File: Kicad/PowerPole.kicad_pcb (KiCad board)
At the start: 2 copper layers, 198.1 x 116.8 mm, 41 parts, among them J1 Anderson powerpole, J2 Anderson powerpole, J3 Anderson powerpole, J4 Anderson powerpole, J5 Anderson powerpole, K1 896HP-1AH-C-12VDC, SW1 SW_Push

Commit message: PCB update
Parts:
- added J6: Meter +ve, Connector_Wire:SolderWire-0.5sqmm_1x01_D0.9mm_OD2.1mm, F.Cu at (124.5, 45.7)
- added J7: Meter GND, Connector_Wire:SolderWire-2.5sqmm_1x01_D2.4mm_OD4.4mm, F.Cu at (98.4, 57.8)
- added J8: Meter LOAD, Connector_Wire:SolderWire-2.5sqmm_1x01_D2.4mm_OD4.4mm, F.Cu at (108.0, 57.8)
- moved D3 86.0 mm to (187.3, 77.5), turned to 90 degrees
- moved R2 79.9 mm to (187.3, 66.7), turned to 90 degrees
- moved D2 74.3 mm to (183.5, 38.1), turned to 0 degrees
- moved R1 73.3 mm to (193.7, 67.3)
- moved C2 67.9 mm to (194.3, 38.1)
- moved C1 60.3 mm to (193.0, 57.1)
- moved C4 51.7 mm to (184.8, 52.1), turned to 90 degrees
- moved D7 51.6 mm to (168.9, 85.1)
- moved D9 51.6 mm to (127.0, 85.1)
- moved F4 51.6 mm to (139.7, 85.1)
- moved F5 51.6 mm to (158.8, 85.1)
- moved D10 51.6 mm to (108.0, 85.1)
- moved F2 51.6 mm to (97.8, 85.1)
- moved D8 51.6 mm to (149.9, 85.1)
- moved F3 51.6 mm to (116.8, 85.1)
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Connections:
- net Net-(D1-Pad2) renamed /Vout
- C1 pad 2: Net-(C1-Pad2) -> /GND
- C2 pad 2: Net-(C1-Pad2) -> /GND
- C3 pad 2: Net-(C1-Pad2) -> /GND
- C4 pad 2: Net-(C1-Pad2) -> /GND
- C5 pad 2: Net-(C1-Pad2) -> /GND
- D1 pad 1: Net-(C1-Pad2) -> /GND
- D10 pad 1: Net-(C1-Pad2) -> /GND
- D13 pad 2: Net-(C1-Pad2) -> /GND
- D15 pad 1: Net-(C1-Pad2) -> /GND
- D2 pad 1: Net-(C1-Pad2) -> /GND
- D4 pad 2: Net-(C1-Pad2) -> /GND
- D5 pad 2: Net-(C1-Pad2) -> /GND
- D6 pad 1: Net-(C1-Pad2) -> /GND
- D7 pad 1: Net-(C1-Pad2) -> /GND
- D8 pad 1: Net-(C1-Pad2) -> /GND
- D9 pad 1: Net-(C1-Pad2) -> /GND
- J1 pad 2: Net-(C1-Pad2) -> Net-(J1-Pad2)
- J2 pad 2: Net-(C1-Pad2) -> /GND
- J3 pad 2: Net-(C1-Pad2) -> /GND
- J4 pad 2: Net-(C1-Pad2) -> /GND
- J5 pad 2: Net-(C1-Pad2) -> /GND
- K1 pad 85: Net-(C1-Pad2) -> /GND
- R1 pad 2: Net-(C1-Pad2) -> /GND
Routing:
- net Net-(D14-Pad2): track 96.8 -> 42.7 mm
- net Net-(C1-Pad1): track 136.9 -> 92.3 mm
- net Net-(F4-Pad1): track 0.00 -> 32.2 mm
- net Net-(F3-Pad1): track 0.00 -> 32.2 mm
- net Net-(F5-Pad1): track 0.00 -> 32.2 mm
- net Net-(F2-Pad1): track 0.00 -> 31.5 mm
- net Net-(J1-Pad2): track 0.00 -> 18.0 mm
- net /Vout: track 12.3 -> 0.00 mm
- net Net-(F1-Pad1): track 20.2 -> 23.9 mm
- net Net-(D9-Pad2): track 6.66 -> 3.81 mm
- net Net-(D8-Pad2): track 6.66 -> 3.81 mm
- net Net-(D7-Pad2): track 6.66 -> 3.81 mm
- net Net-(D11-Pad1): track 24.8 -> 22.5 mm
- net Net-(D10-Pad2): track 6.66 -> 4.44 mm
- net Net-(D11-Pad2): track 23.2 -> 21.1 mm
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- added copper zone on F.Cu, net (none)
- added copper zone on B.Cu, net /GND
- removed copper zone on B.Cu, net Net-(C1-Pad2)
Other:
- board size 198.1 x 116.8 mm -> 113 x 102.9 mm

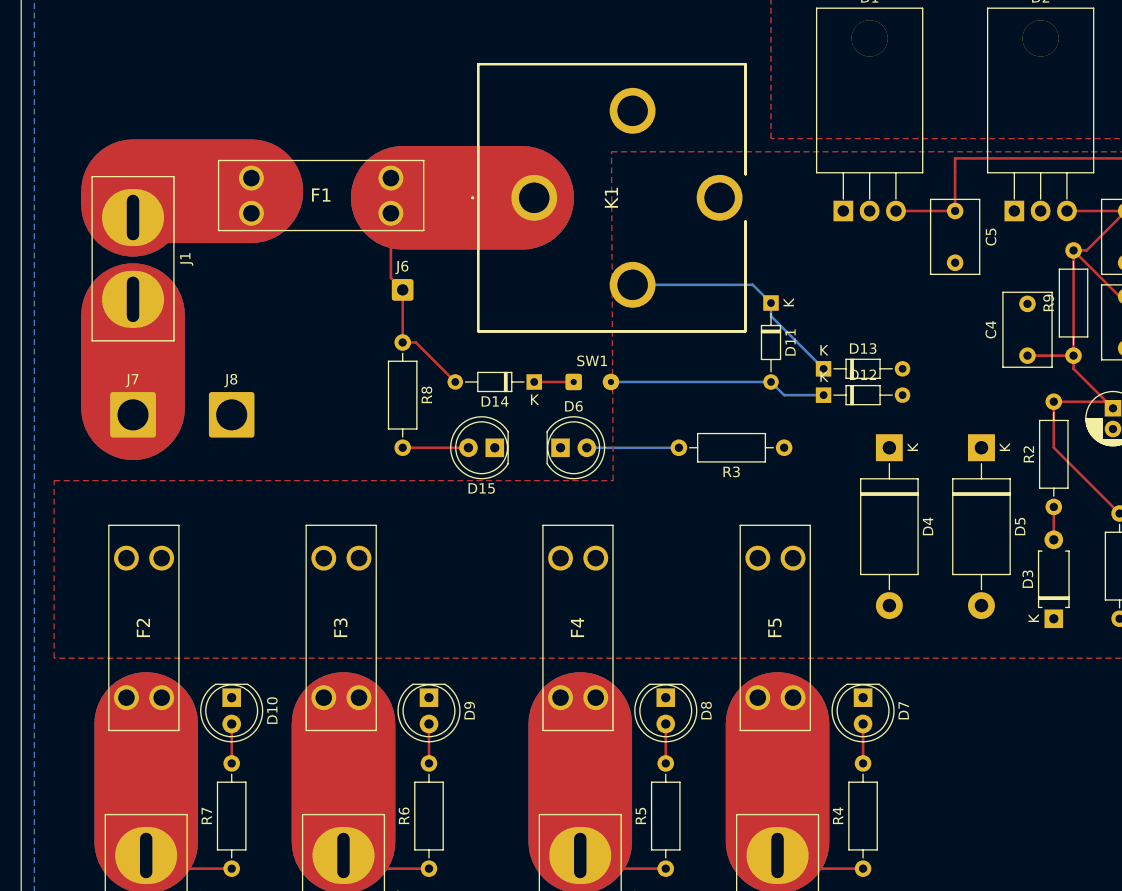
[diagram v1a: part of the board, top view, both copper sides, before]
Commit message: PCB silkscreen update
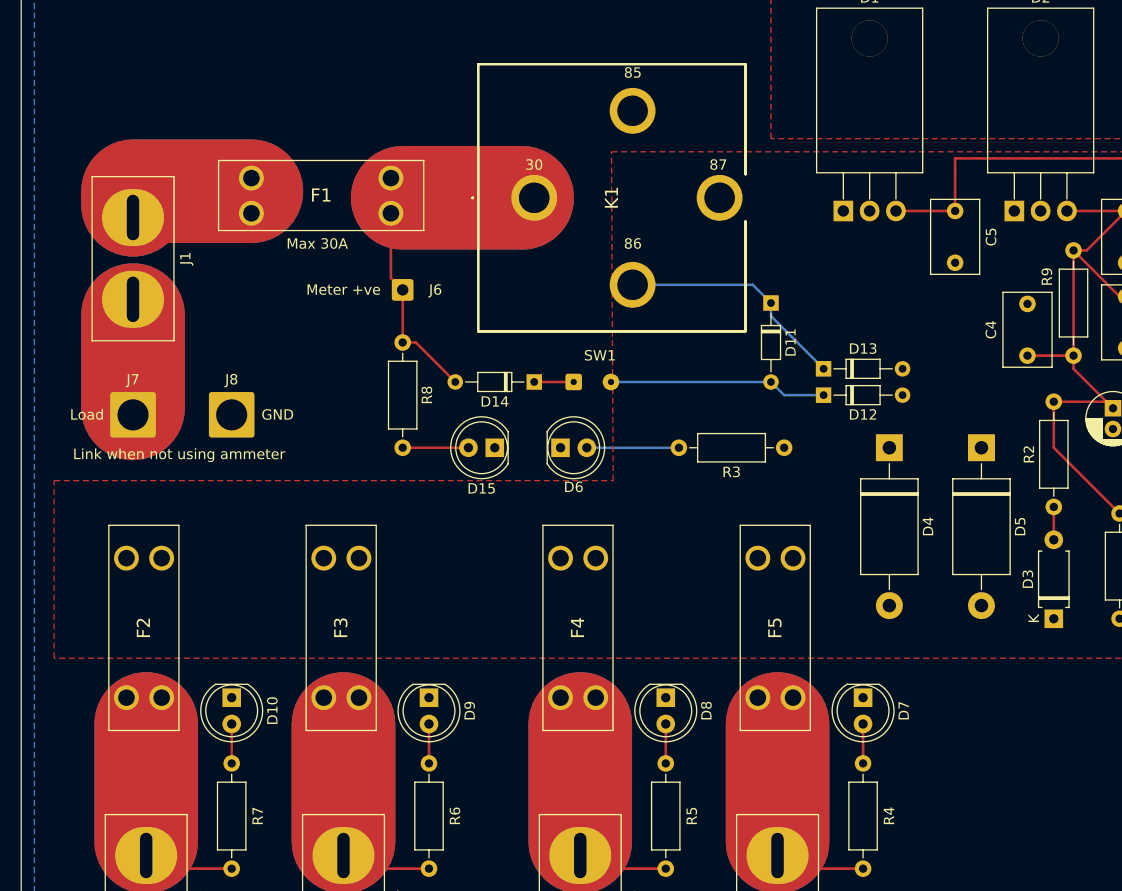
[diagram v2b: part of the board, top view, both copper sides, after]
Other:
- board text added: "30"
- board text added: "85"
- board text added: "86"
- board text added: "87"
- board text added: "GND"
- board text added: "Link when not using ammeter"
- board text added: "Load"
- board text added: "Max 30A"
- board text added: "Meter +ve"

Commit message: Added open source logo to pcb
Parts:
- added G***: LOGO, OpenSourceLogos:ohs-logo, F.Cu at (185.4, 88.9)
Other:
- board text added: "https://bit.ly/3gsBUNr"

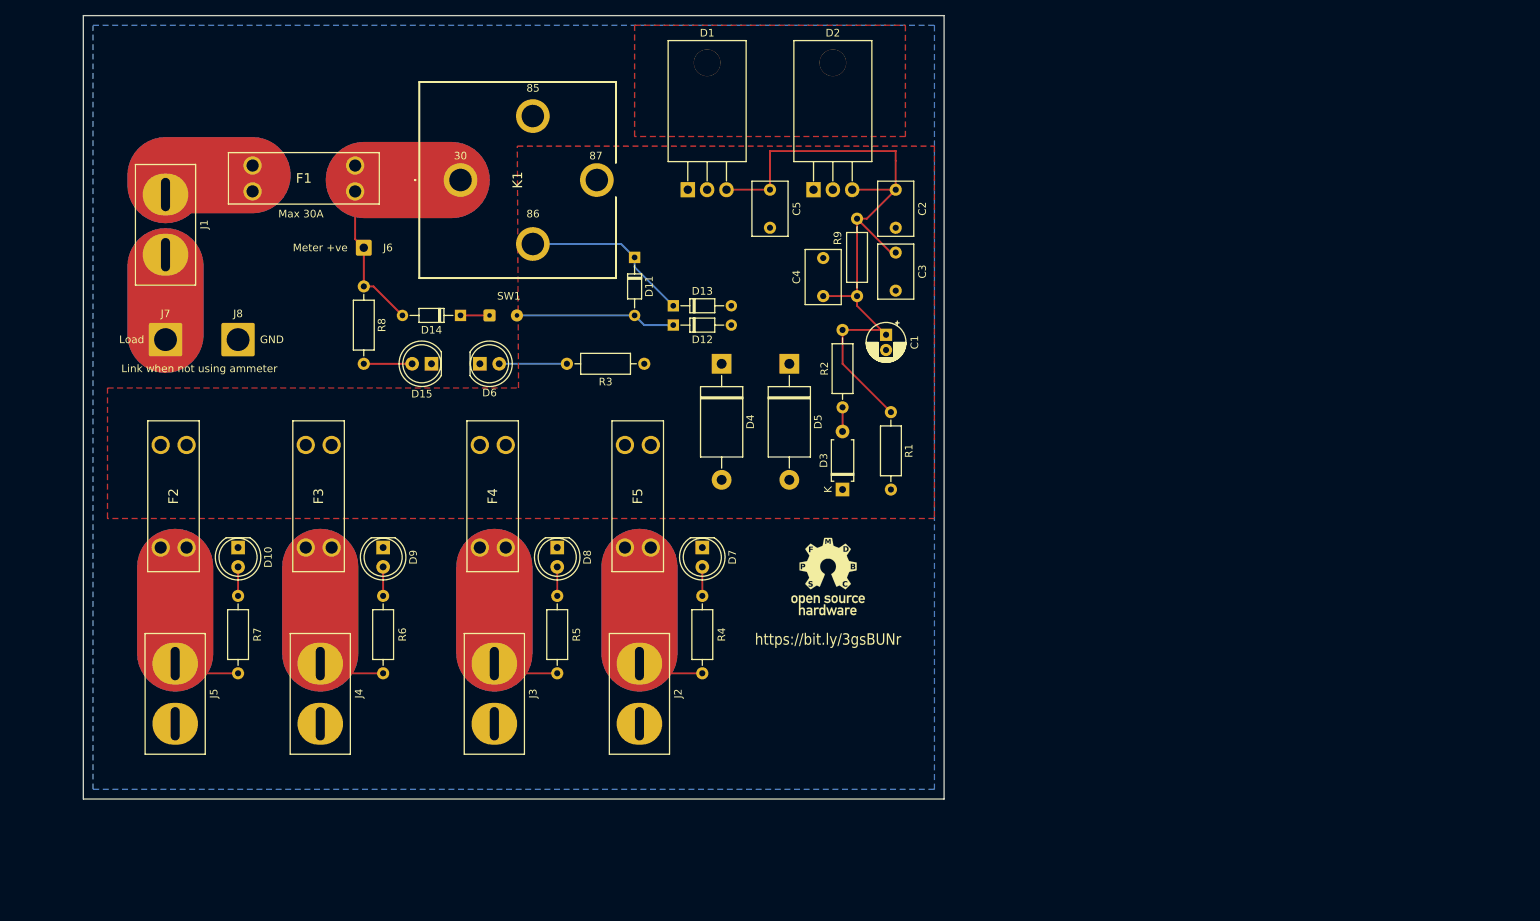
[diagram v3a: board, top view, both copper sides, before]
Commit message: Added mounting holes
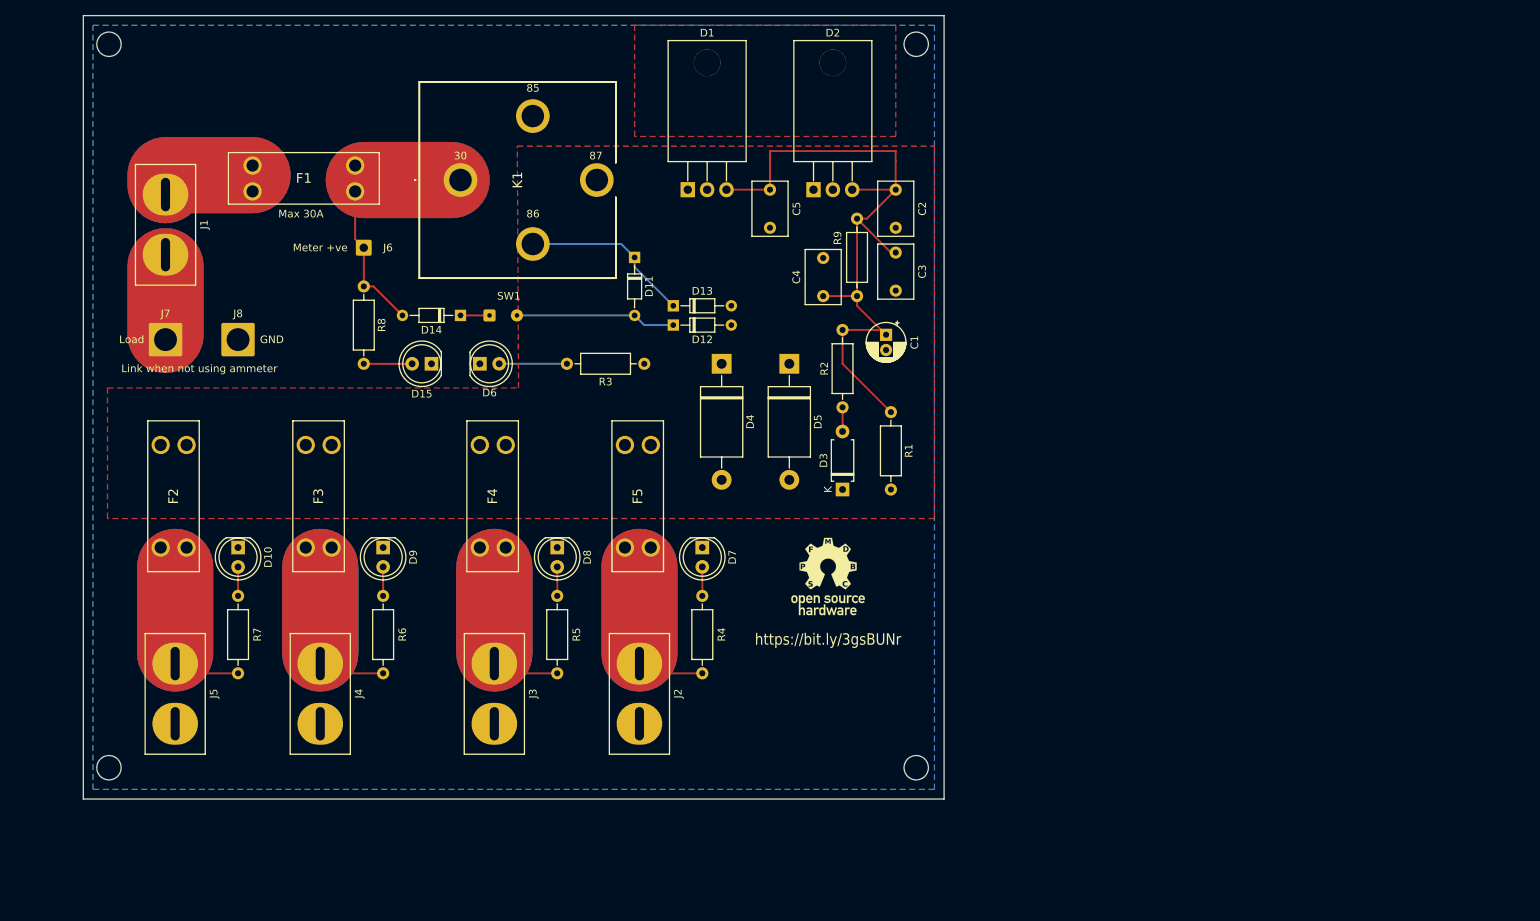
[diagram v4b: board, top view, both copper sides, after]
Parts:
- added  : MountingHole_3.2mm_M3, MountingHole:MountingHole_3.2mm_M3, F.Cu at (91.0, 114.0)
- added  : MountingHole_3.2mm_M3, MountingHole:MountingHole_3.2mm_M3, F.Cu at (197.0, 19.0)
- added  : MountingHole_3.2mm_M3, MountingHole:MountingHole_3.2mm_M3, F.Cu at (197.0, 114.0)
- added  : MountingHole_3.2mm_M3, MountingHole:MountingHole_3.2mm_M3, F.Cu at (91.0, 19.0)
